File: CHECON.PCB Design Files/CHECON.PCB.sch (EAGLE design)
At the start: 48 parts, among them U2 MAX232SOIC16, U3 RS485SOIC

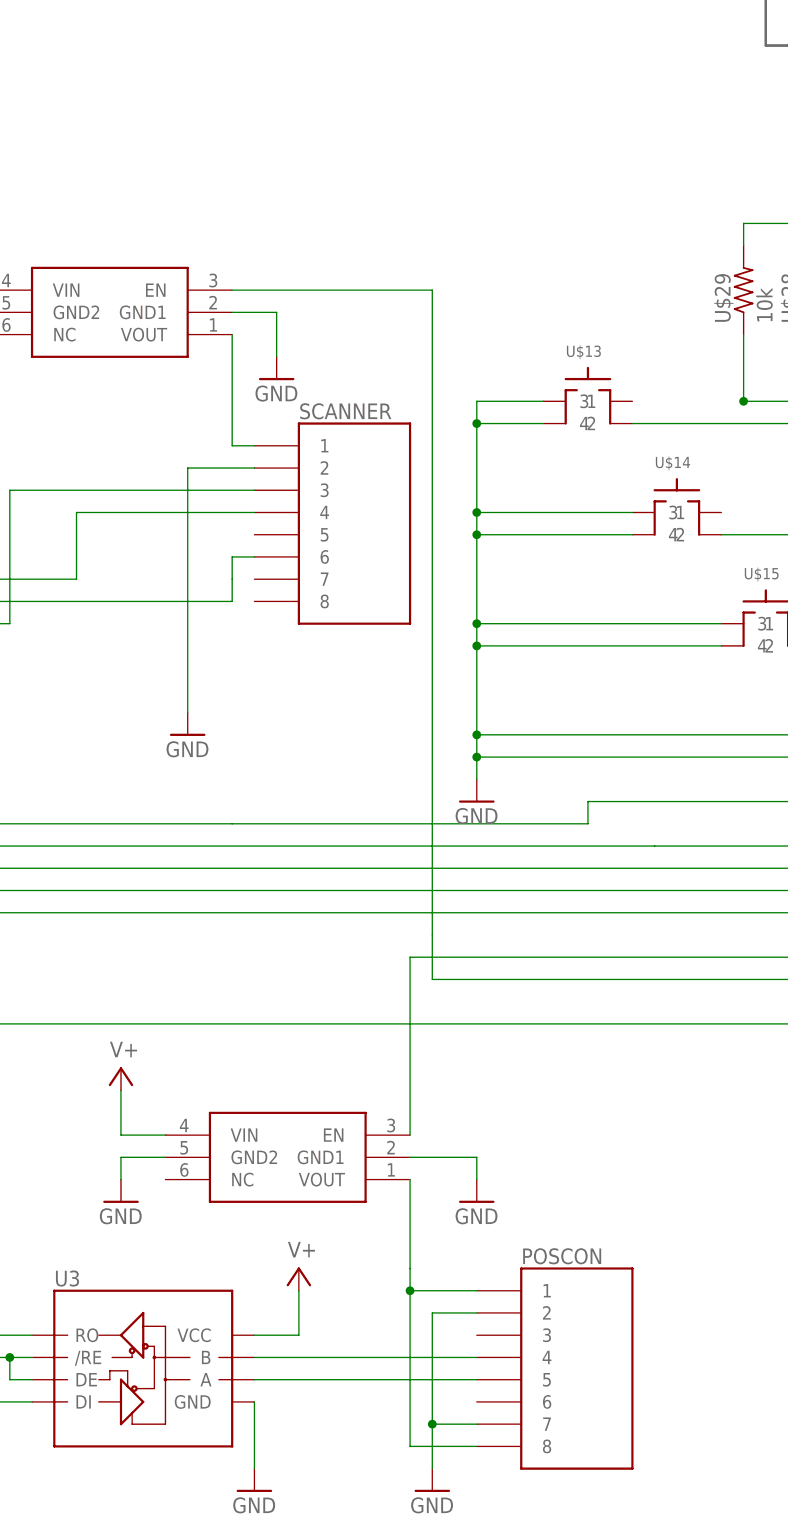
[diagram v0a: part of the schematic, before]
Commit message: Pull-ups and terminator
Added pull-ups to Micrel switches and RS485 Bus terminator
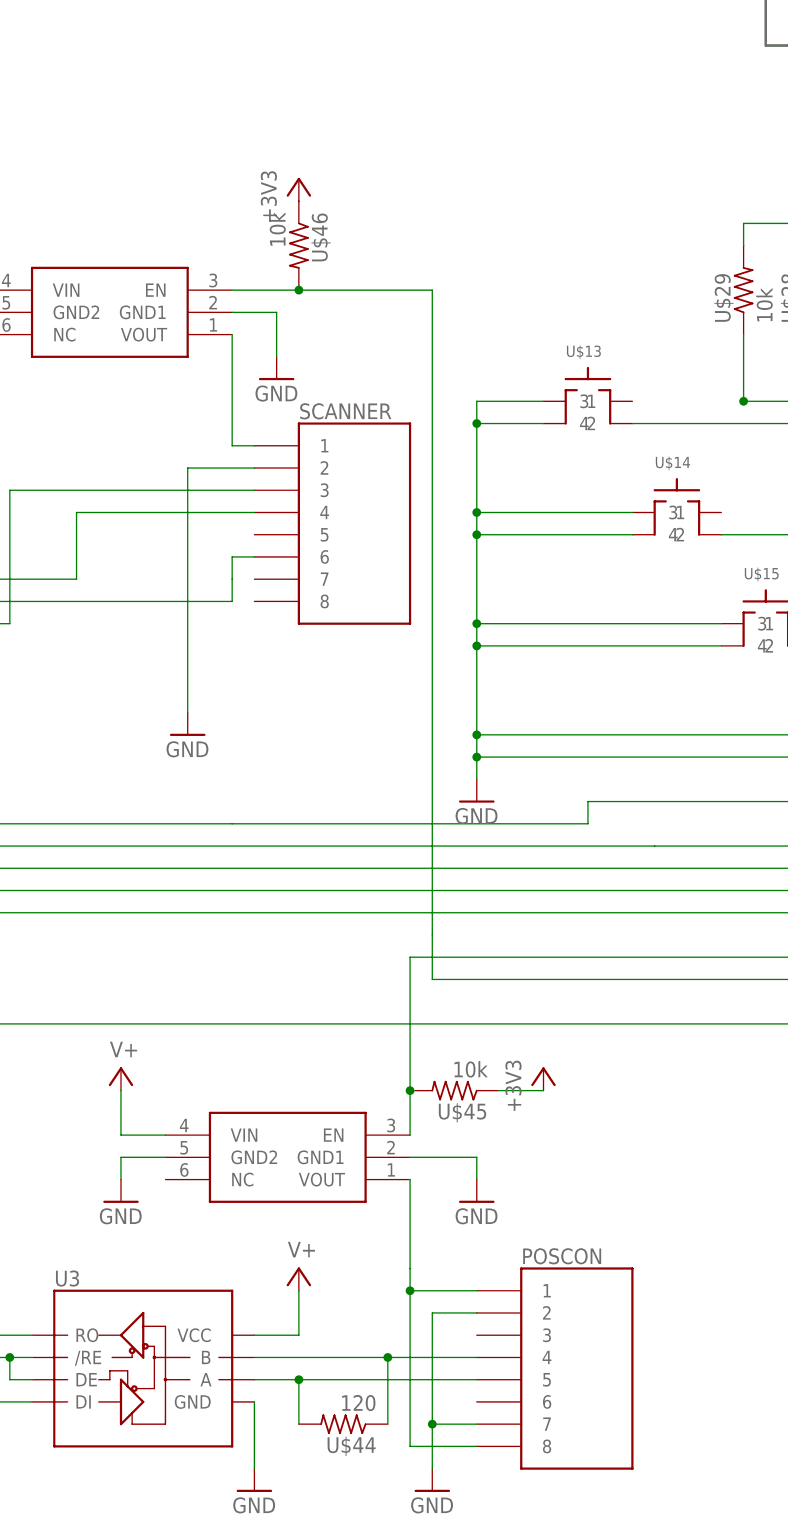
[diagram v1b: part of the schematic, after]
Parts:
- added U$44: 120, GW-devices:RF-R0805
- added U$45, U$46: 10k, GW-devices:RF-R0805
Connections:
- net +3V3: now also U$45.1, U$46.1
- net N$19: now also U$44.1
- net N$20: now also U$44.2
- net N$39: now also U$45.2
- net N$40: now also U$46.2
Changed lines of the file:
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@@
 <attribute name="NOTES" value="DNP"/>
 </part>
+<part name="U$44" library="GW-devices" deviceset="RF-R" device="0805" value="120">
+<attribute name="MFGN" value="Vishay Dale"/>
+<attribute name="MFGP" value="CRCW080510K0FKEA"/>
+</part>
+<part name="U$45" library="GW-devices" deviceset="RF-R" device="0805" value="10k">
+<attribute name="MFGN" value="Vishay Dale"/>
+<attribute name="MFGP" value="CRCW080510K0FKEA"/>
+</part>
+<part name="U$46" library="GW-devices" deviceset="RF-R" device="0805" value="10k">
+<attribute name="MFGN" value="Vishay Dale"/>
+<attribute name="MFGP" value="CRCW080510K0FKEA"/>
+</part>
+<part name="+3V4" library="supply1" deviceset="+3V3" device=""/>
+<part name="+3V5" library="supply1" deviceset="+3V3" device=""/>
 </parts>
 <sheets>
@@
 <attribute name="NOTES" x="-86.36" y="218.44" size="1.778" layer="96" display="off"/>
 </instance>
+<instance part="U$44" gate="G$1" x="-309.88" y="53.34" rot="R180">
+<attribute name="MFGP" x="-309.88" y="53.34" size="1.778" layer="96" rot="R180" display="off"/>
+<attribute name="MFGN" x="-309.88" y="53.34" size="1.778" layer="96" rot="R180" display="off"/>
+</instance>
+<instance part="U$45" gate="G$1" x="-297.18" y="91.44" rot="R180">
+<attribute name="MFGP" x="-297.18" y="91.44" size="1.778" layer="96" rot="R180" display="off"/>
+<attribute name="MFGN" x="-297.18" y="91.44" size="1.778" layer="96" rot="R180" display="off"/>
+</instance>
+<instance part="U$46" gate="G$1" x="-314.96" y="187.96" rot="R270">
+<attribute name="MFGP" x="-314.96" y="187.96" size="1.778" layer="96" rot="R270" display="off"/>
+<attribute name="MFGN" x="-314.96" y="187.96" size="1.778" layer="96" rot="R270" display="off"/>
+</instance>
+<instance part="+3V4" gate="G$1" x="-314.96" y="195.58"/>
+<instance part="+3V5" gate="G$1" x="-287.02" y="93.98"/>
 </instances>
 <busses>
@@
 <pinref part="U$21" gate="G$1" pin="1"/>
 <pinref part="+3V2" gate="G$1" pin="+3V3"/>
+</segment>
+<segment>
+<pinref part="U$46" gate="G$1" pin="1"/>
+<pinref part="+3V4" gate="G$1" pin="+3V3"/>
+</segment>
+<segment>
+<pinref part="U$45" gate="G$1" pin="1"/>
+<pinref part="+3V5" gate="G$1" pin="+3V3"/>
+<wire x1="-292.1" y1="91.44" x2="-287.02" y2="91.44" width="0.1524" layer="91"/>
 </segment>
 </net>
@@
 <pinref part="U3" gate="G$1" pin="B"/>
 <pinref part="POSCON" gate="G$1" pin="4"/>
-<wire x1="-320.04" y1="60.96" x2="-294.64" y2="60.96" width="0.1524" layer="91"/>
+<wire x1="-320.04" y1="60.96" x2="-304.8" y2="60.96" width="0.1524" layer="91"/>
+<pinref part="U$44" gate="G$1" pin="1"/>
+<wire x1="-304.8" y1="60.96" x2="-294.64" y2="60.96" width="0.1524" layer="91"/>
+<wire x1="-304.8" y1="53.34" x2="-304.8" y2="60.96" width="0.1524" layer="91"/>
+<junction x="-304.8" y="60.96"/>
 </segment>
 </net>
@@
 <pinref part="U3" gate="G$1" pin="A"/>
 <pinref part="POSCON" gate="G$1" pin="5"/>
-<wire x1="-320.04" y1="58.42" x2="-294.64" y2="58.42" width="0.1524" layer="91"/>
+<wire x1="-320.04" y1="58.42" x2="-314.96" y2="58.42" width="0.1524" layer="91"/>
+<pinref part="U$44" gate="G$1" pin="2"/>
+<wire x1="-314.96" y1="58.42" x2="-294.64" y2="58.42" width="0.1524" layer="91"/>
+<wire x1="-314.96" y1="53.34" x2="-314.96" y2="58.42" width="0.1524" layer="91"/>
+<junction x="-314.96" y="58.42"/>
 </segment>
 </net>
@@
 <segment>
 <pinref part="U$5" gate="G$1" pin="EN"/>
-<wire x1="-302.26" y1="86.36" x2="-302.26" y2="106.68" width="0.1524" layer="91"/>
+<wire x1="-302.26" y1="86.36" x2="-302.26" y2="91.44" width="0.1524" layer="91"/>
 <pinref part="U$10" gate="G$1" pin="PTD4/LLWU_P14/MADC0_SE21/SPI0_PCS1/!UART0_RTS!/FTM0_CH4/EWM_IN/GPIO_BSM_FRAME"/>
+<wire x1="-302.26" y1="91.44" x2="-302.26" y2="106.68" width="0.1524" layer="91"/>
 <wire x1="-302.26" y1="106.68" x2="-190.5" y2="106.68" width="0.1524" layer="91"/>
+<pinref part="U$45" gate="G$1" pin="2"/>
+<junction x="-302.26" y="91.44"/>
 </segment>
 </net>
@@
 <segment>
 <pinref part="U$4" gate="G$1" pin="EN"/>
-<wire x1="-322.58" y1="182.88" x2="-299.72" y2="182.88" width="0.1524" layer="91"/>
+<wire x1="-322.58" y1="182.88" x2="-314.96" y2="182.88" width="0.1524" layer="91"/>
+<wire x1="-314.96" y1="182.88" x2="-299.72" y2="182.88" width="0.1524" layer="91"/>
 <wire x1="-299.72" y1="182.88" x2="-299.72" y2="109.22" width="0.1524" layer="91"/>
 <pinref part="U$10" gate="G$1" pin="PTD3/SPI0_SIN/UART2_TX/I2C0_SCL/GPIO5_BSM_CLK"/>
 <wire x1="-190.5" y1="104.14" x2="-299.72" y2="104.14" width="0.1524" layer="91"/>
 <wire x1="-299.72" y1="104.14" x2="-299.72" y2="109.22" width="0.1524" layer="91"/>
-</segment>
-</net>
+<pinref part="U$46" gate="G$1" pin="2"/>
+<junction x="-314.96" y="182.88"/>
+</segment>
+</net>
